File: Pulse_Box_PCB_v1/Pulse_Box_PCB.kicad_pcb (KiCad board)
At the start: 2 copper layers, 40 x 50 mm, 35 parts, among them J1 Barrel_Jack, J2 Conn_02x05_Odd_Even, J3 USB_B_Micro, J4 Conn_01x03_Pin, U1 STM32F407VGTx, U2 SN74LV1T34DBV, U3 AP2112K-3.3, U4 TPSM53604RDA, Y1 8MHz Crystal

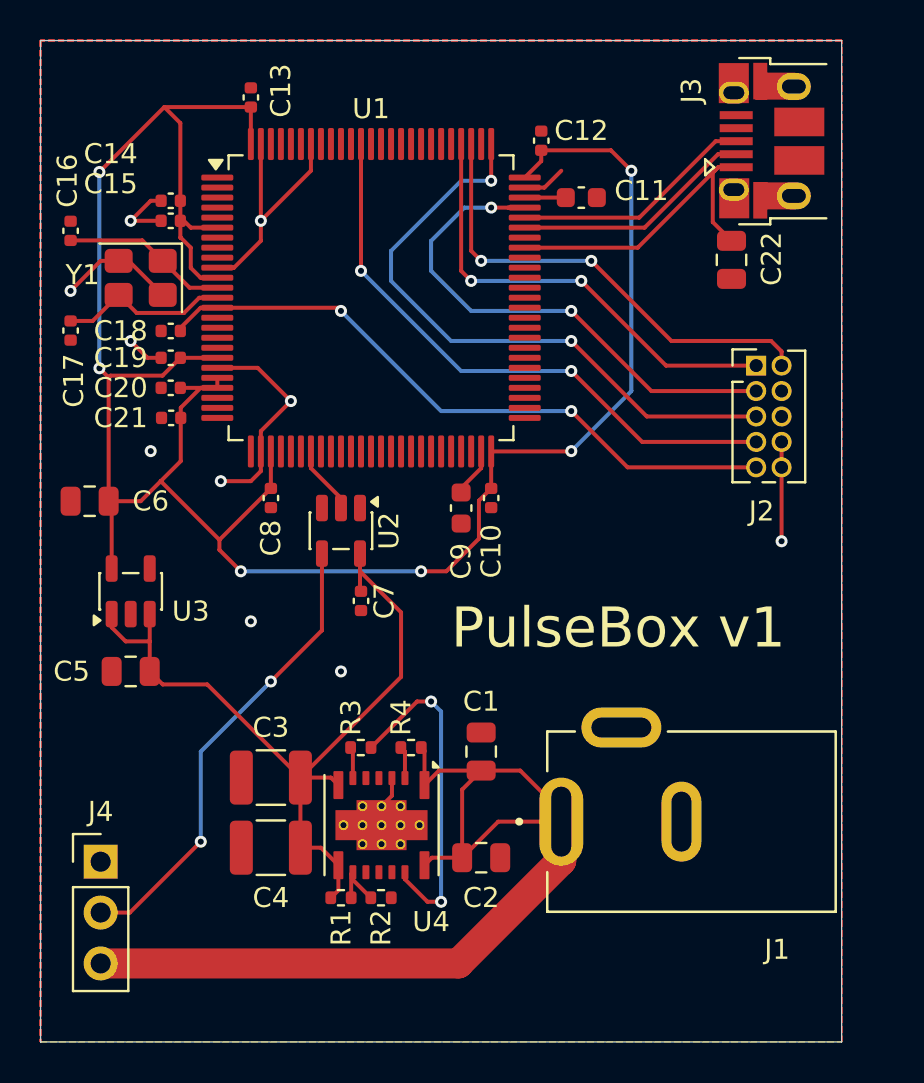
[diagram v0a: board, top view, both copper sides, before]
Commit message: add v2 board design with esp32-s3 wroom module, moved versions into dedicated directories
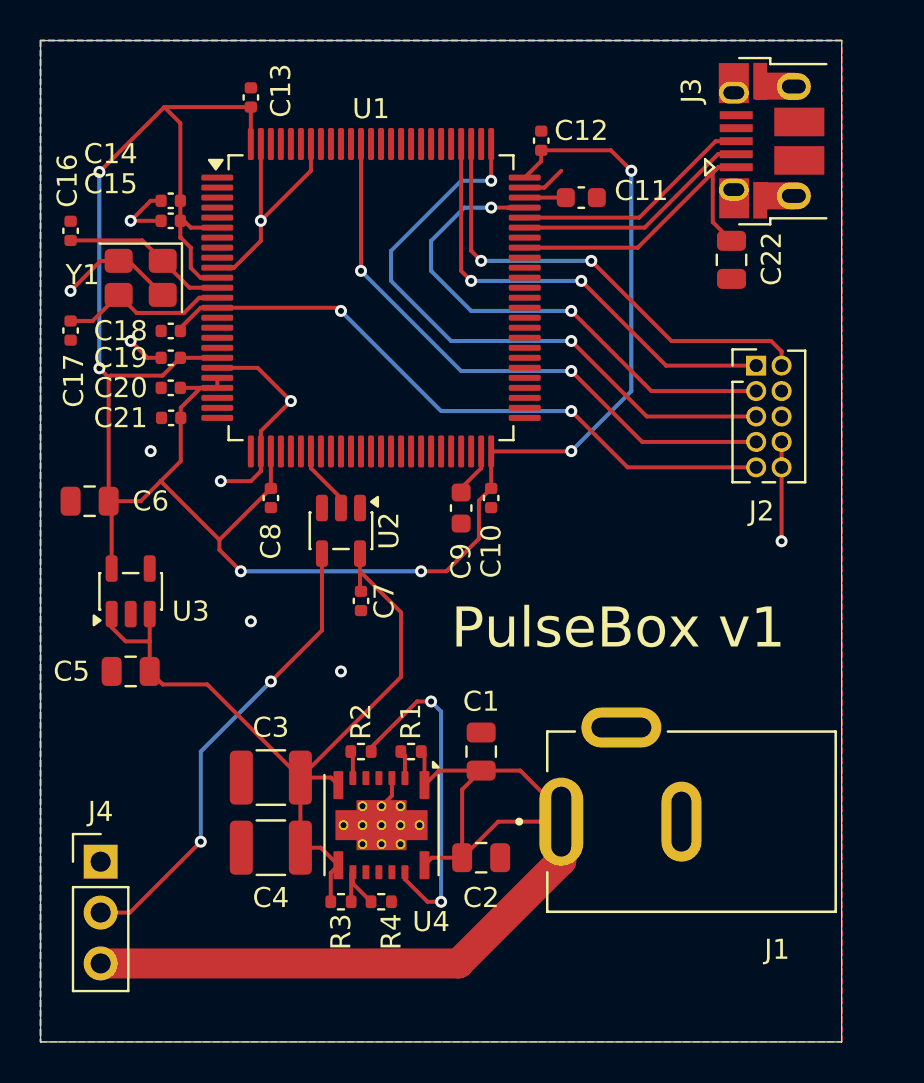
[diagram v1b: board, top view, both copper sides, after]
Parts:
- moved R1 8.10 mm to (110.0, 88.5), turned to 180 degrees
- moved R4 7.84 mm to (108.5, 96.0), turned to 0 degrees
- moved R3 7.76 mm to (106.5, 96.0), turned to 0 degrees
- moved R2 7.37 mm to (107.5, 88.5), turned to 180 degrees
- turned C13 to -90 degrees
- turned C19 to 0 degrees
- turned C8 to 90 degrees
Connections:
- C20 pad 2: Net-(U1-VDDA) -> +3.3V
- C21 pad 1: Net-(U1-VDDA) -> +3.3V
- U1 pad 22: Net-(U1-VDDA) -> +3.3V
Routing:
- net GND: track 41.3 -> 43.2 mm, vias 9 -> 10
- net +3.3V: track 117.0 -> 115.2 mm, vias 7 -> 6
